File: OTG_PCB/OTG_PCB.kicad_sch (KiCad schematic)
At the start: 14 parts, among them J1 USB_C_Receptacle_USB2.0, J2 USB_MINI_B, J3 USB_A, J4 USB_MINI_B, J5 USB_C_Receptacle_USB2.0, U1 USB3740B-AI2, U2 TUSB320IRWBR

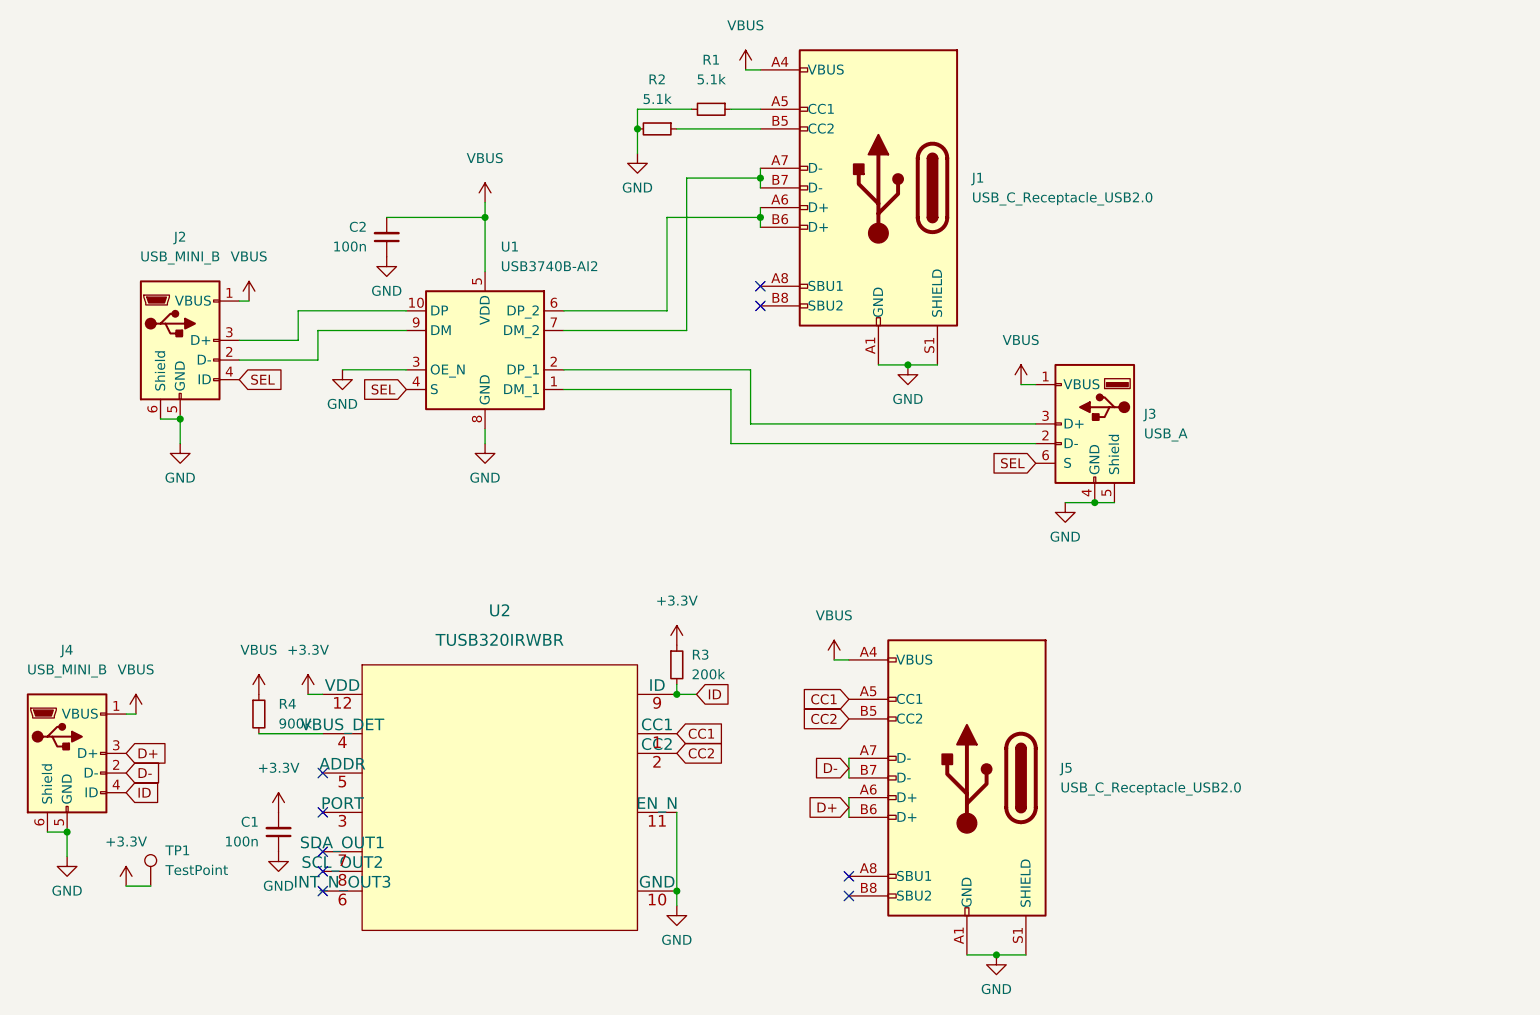
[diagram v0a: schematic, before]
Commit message: Single layer, flex only
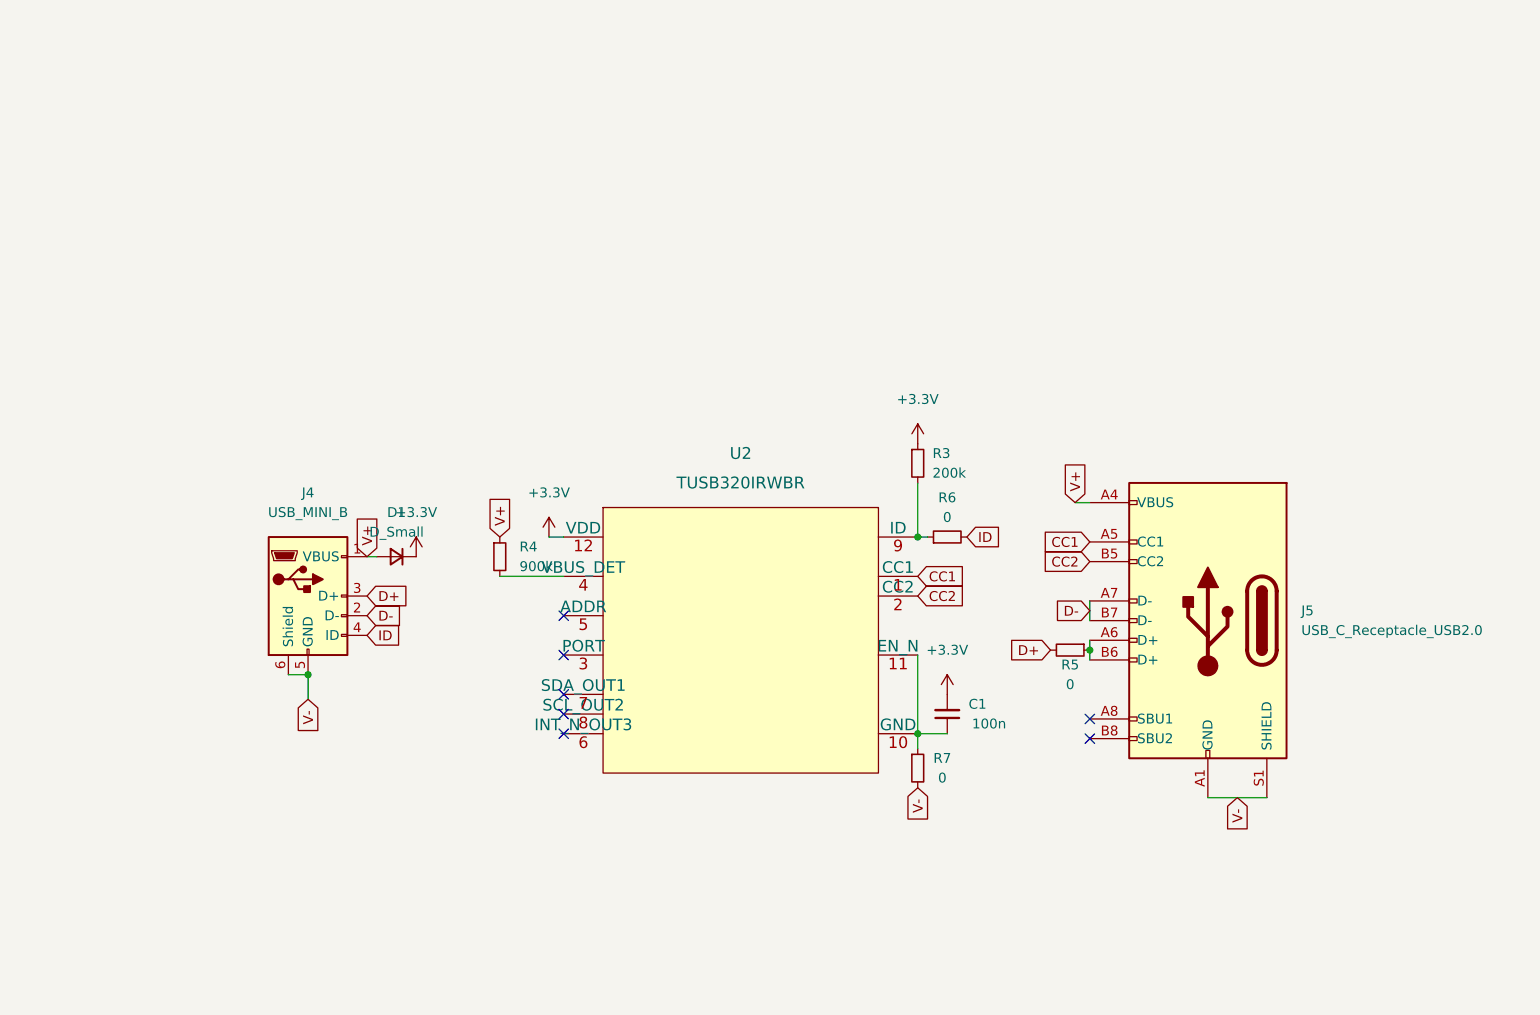
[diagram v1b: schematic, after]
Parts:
- removed C2: 100n, Capacitor_SMD:C_0402_1005Metric_Pad0.74x0.62mm_HandSolder, symbol Device:C_Small
- removed J1: USB_C_Receptacle_USB2.0, Connector_USB:USB_C_Receptacle_HRO_TYPE-C-31-M-12, symbol Connector:USB_C_Receptacle_USB2.0
- removed J2: USB_MINI_B, Connector_USB:USB_Mini-B_Wuerth_65100516121_Horizontal, symbol Connector:USB_OTG
- removed J3: USB_A, Connector_USB:USB_A_Wuerth_614004134726_Horizontal, symbol Connector:USB_A
- removed R1, R2: 5.1k, Resistor_SMD:R_0402_1005Metric_Pad0.72x0.64mm_HandSolder, symbol Device:R_Small
- removed TP1: TestPoint, TestPoint:TestPoint_Pad_D2.0mm, symbol Connector:TestPoint
- removed U1: USB3740B-AI2, Package_DFN_QFN:UQFN-10_1.3x1.8mm_P0.4mm, symbol Interface_USB:USB3740B-AI2
- added D1: D_Small, Diode_SMD:D_SOD-123, symbol Device:D_Small
- added R5, R6, R7: 0, Resistor_SMD:R_1206_3216Metric, symbol Device:R_Small
- C1: footprint Capacitor_SMD:C_0402_1005Metric_Pad0.74x0.62mm_HandSolder -> Capacitor_SMD:C_0603_1608Metric
- R3, R4: footprint Resistor_SMD:R_0402_1005Metric_Pad0.72x0.64mm_HandSolder -> Resistor_SMD:R_0603_1608Metric
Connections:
- net +3V3: now also D1.1 (K)
- net D+: now also R5.2; no longer J5.A6 (D+), J5.B6 (D+)
- net ID: now also R6.2; no longer R3.2, U2.9 (ID)
- net GND renamed V-
- net V-: now also R7.2; no longer C1.1, U2.10 (GND), U2.11 (EN_N)
- net VBUS renamed V+
- net V+: now also D1.2 (A)
- new net: J5.A6 (D+), J5.B6 (D+), R5.1
- new net: R3.2, R6.1, U2.9 (ID)
- new net: C1.1, R7.1, U2.10 (GND), U2.11 (EN_N)
- no-connect marks 9 -> 7
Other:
- moved on the sheet: C1, J4, J5, R3, R4, U2
